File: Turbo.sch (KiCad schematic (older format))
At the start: 16 parts, among them U13 74HC74, U14 74HC86, U15 74HC74

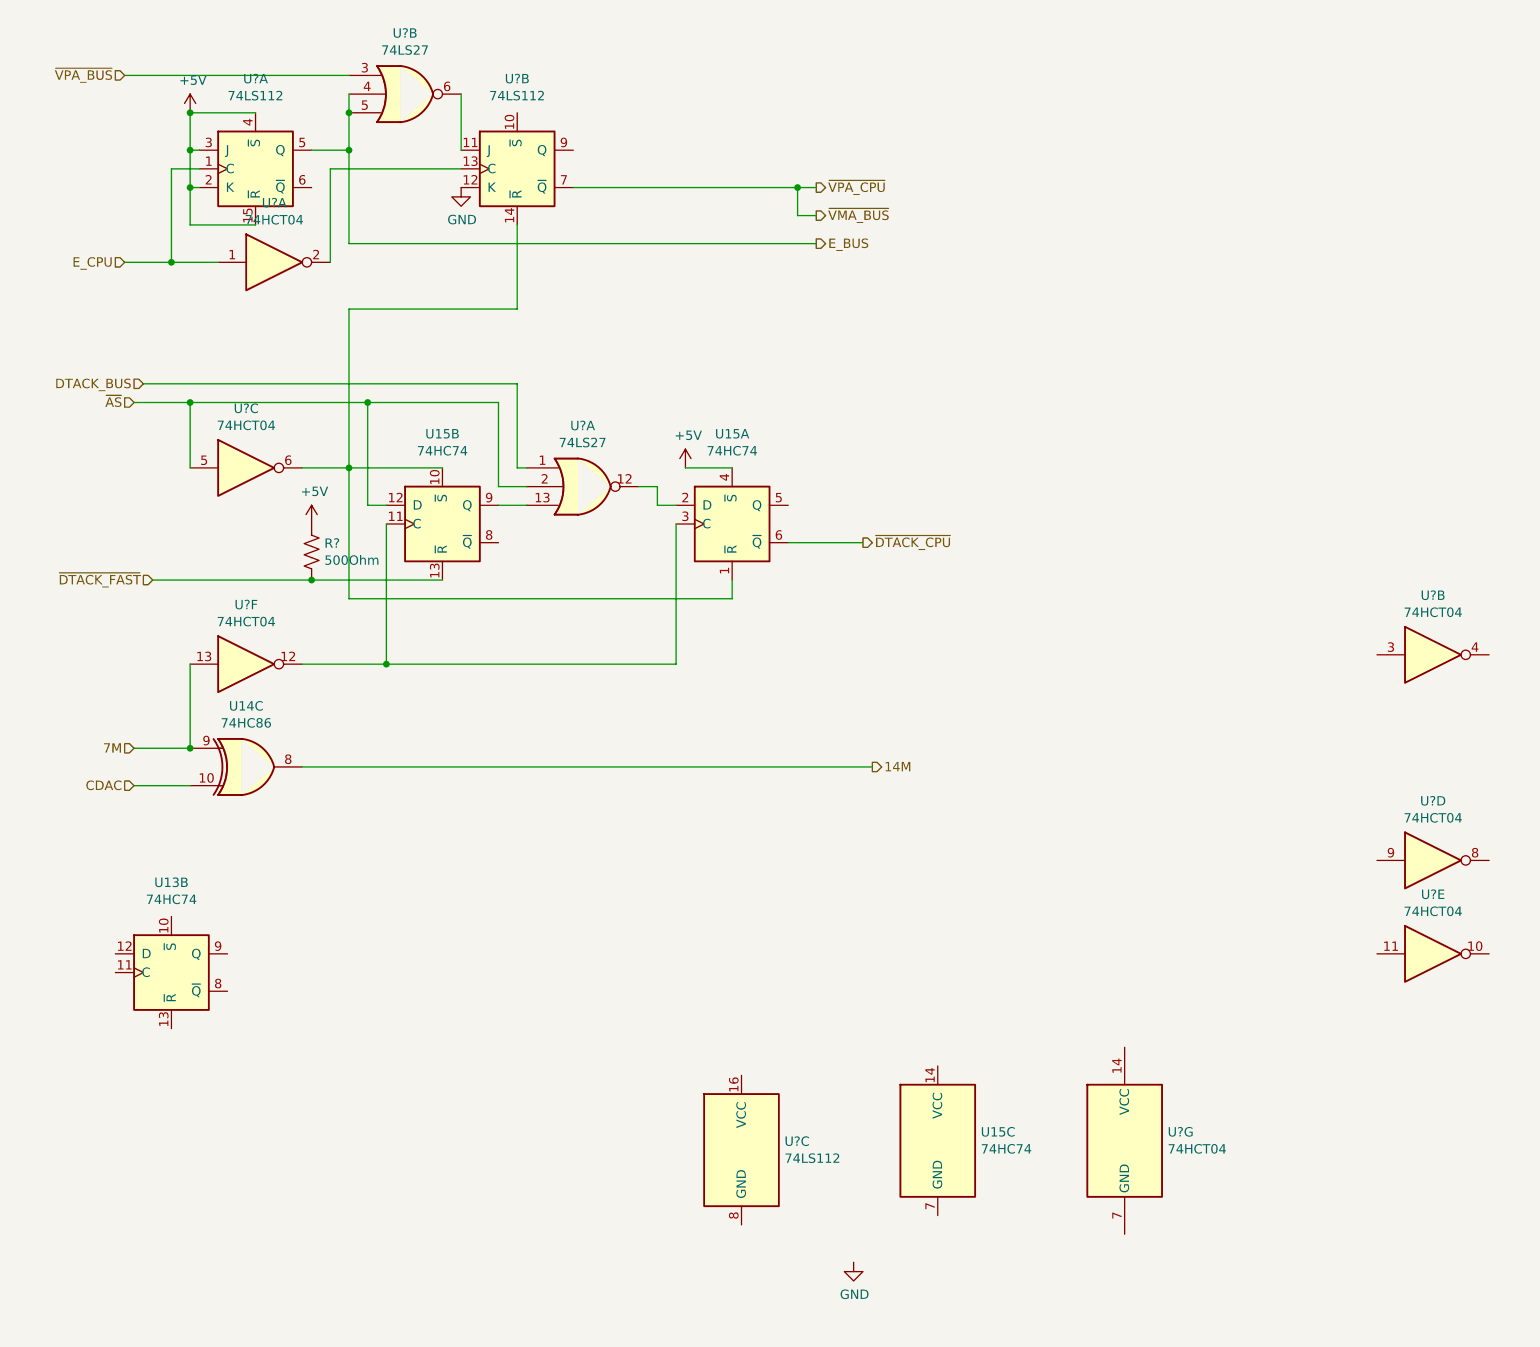
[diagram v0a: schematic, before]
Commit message: finish turbo section
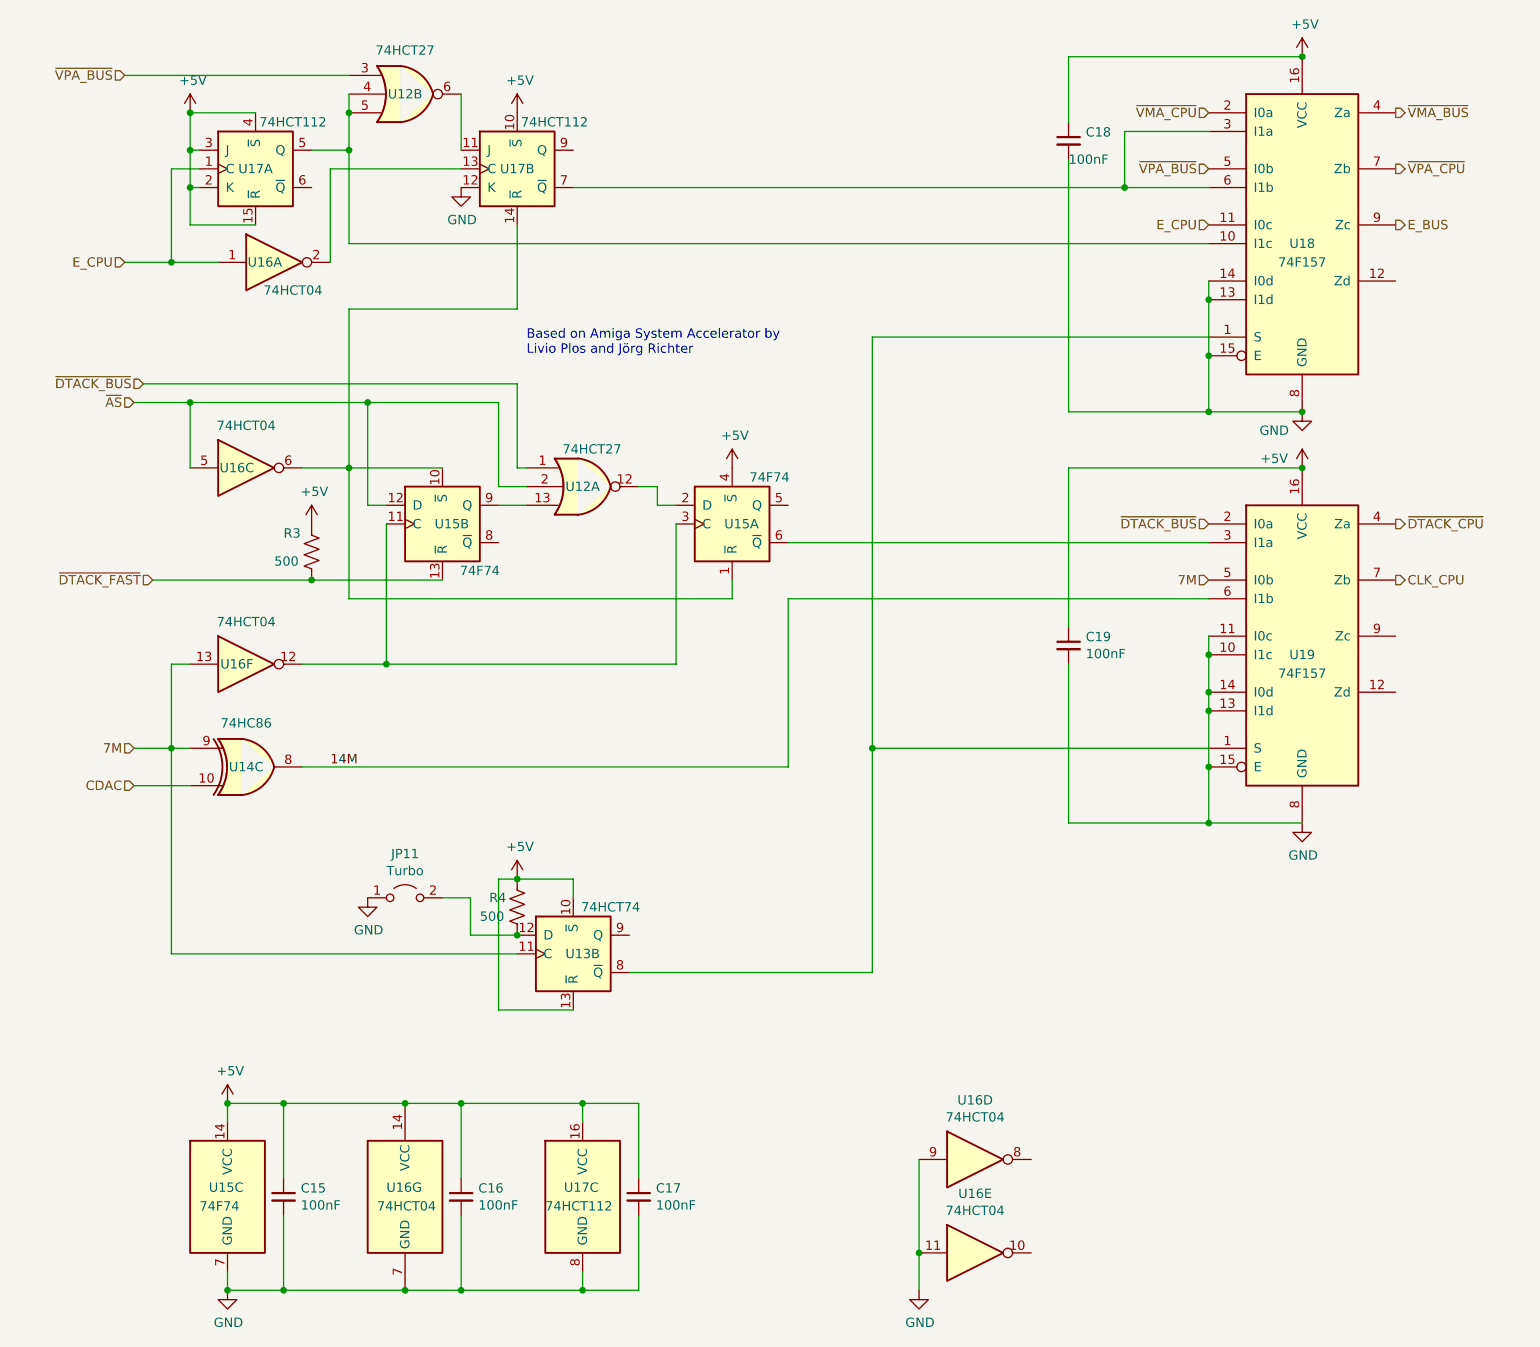
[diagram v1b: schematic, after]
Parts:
- removed U?: 74HCT04, symbol 74:74HCT04
- added C15, C16, C17, C18, C19: 100nF, symbol device:C_Small
- added JP11: Turbo, symbol jumper:Jumper_2_Open
- added R4: 500, symbol device:R_US
- added U18, U19: 74F157, symbol 74:74LS157
- R3: renamed from R?; value 500Ohm -> 500
- U12: renamed from U?; value 74LS27 -> 74HCT27
- U13: value 74HC74 -> 74HCT74
- U15: value 74HC74 -> 74F74
- U17: renamed from U?; value 74LS112 -> 74HCT112
- gave numbers to parts that had none: 1
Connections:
- net +5V: now also U13.10 (~S), U13.13 (~R), U15.14 (VCC), U16.14 (VCC), U17.10 (~S), U17.16 (VCC), C15.1, C16.1, C17.1, C18.1, C19.1, R4.1, U18.16 (VCC), U19.16 (VCC)
- net 14M: now also U19.6 (I1b)
- net 7M: now also U13.11 (C), U19.5 (I0b)
- net E_BUS: now also U18.9 (Zc); no longer U12.4, U12.5, U17.5 (Q)
- net E_CPU: now also U18.11 (I0c)
- net GND: now also U15.7 (GND), U16.11, U16.7 (GND), U16.9, U17.8 (GND), C15.2, C16.2, C17.2, C18.2, C19.2, JP11.1 (A), U18.13 (I1d), U18.14 (I0d), U18.15 (E), U18.8 (GND), U19.10 (I1c), U19.11 (I0c), U19.13 (I1d), U19.14 (I0d), U19.15 (E), U19.8 (GND)
- net ~DTACK_CPU: now also U19.4 (Za); no longer U15.6 (~Q)
- net ~VMA_BUS: now also U18.4 (Za); no longer U17.7 (~Q)
- net ~VPA_BUS: now also U18.5 (I0b)
- net at U13.12 (D): now also JP11.2 (B), R4.2
- net at U13.8 (~Q): now also U18.1 (S), U19.1 (S)
- net DTACK_BUS renamed ~DTACK_BUS
- net ~DTACK_BUS: now also U19.2 (I0a)
- new net: U15.6 (~Q), U19.3 (I1a)
- new net: U12.4, U12.5, U17.5 (Q), U18.10 (I1c)
- new net: U17.7 (~Q), U18.3 (I1a), U18.6 (I1b)
- new net CLK_CPU: U19.7 (Zb)
- new net ~VMA_CPU: U18.2 (I0a)
- new net ~VPA_CPU: U18.7 (Zb)
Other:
- note added: "Based on Amiga System Accelerator by\nLivio Plos and Jörg Richter"
- moved on the sheet: U13B, U15C, U16D, U16E, U16G, U17C

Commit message: component names
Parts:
- U14: value 74HC86 -> 74F86
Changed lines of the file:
@@
 P 1650 4700
 F 0 "U14" H 1650 4700 50  0000 C CNN
-F 1 "74HC86" H 1650 4934 50  0000 C CNN
+F 1 "74F86" H 1650 4934 50  0000 C CNN
 F 2 "" H 1650 4700 50  0001 C CNN
 F 3 "http://www.ti.com/lit/gpn/sn74HC86" H 1650 4700 50  0001 C CNN

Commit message: assign footprints
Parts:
- C15, C16, C17, C18, C19: footprint (none) -> Capacitor_THT:C_Disc_D7.0mm_W2.5mm_P5.00mm
- JP11: footprint (none) -> Connector_PinHeader_2.54mm:PinHeader_1x02_P2.54mm_Vertical
- R3, R4: footprint (none) -> Resistor_THT:R_Axial_DIN0411_L9.9mm_D3.6mm_P12.70mm_Horizontal
- U12, U13, U15, U16: footprint (none) -> Package_DIP:DIP-14_W7.62mm
- U14: footprint (none) -> Package_DIP:DIP-14_W7.62mm_Socket
- U17, U18, U19: footprint (none) -> Package_DIP:DIP-16_W7.62mm
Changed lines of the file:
@@
 F 0 "U14" H 1650 4700 50  0000 C CNN
 F 1 "74F86" H 1650 4934 50  0000 C CNN
-F 2 "" H 1650 4700 50  0001 C CNN
+F 2 "Package_DIP:DIP-14_W7.62mm_Socket" H 1650 4700 50  0001 C CNN
 F 3 "http://www.ti.com/lit/gpn/sn74HC86" H 1650 4700 50  0001 C CNN
 	3    1650 4700
@@
 F 0 "U15" H 4300 3400 50  0000 C CNN
 F 1 "74F74" H 4450 3650 50  0000 C CNN
-F 2 "" H 4250 3400 50  0001 C CNN
+F 2 "Package_DIP:DIP-14_W7.62mm" H 4250 3400 50  0001 C CNN
 F 3 "74xx/74hc_hct74.pdf" H 4250 3400 50  0001 C CNN
 	1    4250 3400
@@
 F 0 "U15" H 2750 3400 50  0000 C CNN
 F 1 "74F74" H 2900 3150 50  0000 C CNN
-F 2 "" H 2700 3400 50  0001 C CNN
+F 2 "Package_DIP:DIP-14_W7.62mm" H 2700 3400 50  0001 C CNN
 F 3 "74xx/74hc_hct74.pdf" H 2700 3400 50  0001 C CNN
 	2    2700 3400
@@
 F 0 "U15" H 1450 7050 50  0000 L CNN
 F 1 "74F74" H 1400 6950 50  0000 L CNN
-F 2 "" H 1550 7000 50  0001 C CNN
+F 2 "Package_DIP:DIP-14_W7.62mm" H 1550 7000 50  0001 C CNN
 F 3 "74xx/74hc_hct74.pdf" H 1550 7000 50  0001 C CNN
 	3    1550 7000
@@
 F 0 "U13" H 3450 5700 50  0000 C CNN
 F 1 "74HCT74" H 3600 5950 50  0000 C CNN
-F 2 "" H 3400 5700 50  0001 C CNN
+F 2 "Package_DIP:DIP-14_W7.62mm" H 3400 5700 50  0001 C CNN
 F 3 "74xx/74hc_hct74.pdf" H 3400 5700 50  0001 C CNN
 	2    3400 5700
@@
 F 0 "U16" H 1750 2000 50  0000 C CNN
 F 1 "74HCT04" H 1900 1850 50  0000 C CNN
-F 2 "" H 1800 2000 50  0001 C CNN
+F 2 "Package_DIP:DIP-14_W7.62mm" H 1800 2000 50  0001 C CNN
 F 3 "https://assets.nexperia.com/documents/data-sheet/74HC_HCT04.pdf" H 1800 2000 50  0001 C CNN
 	1    1800 2000
@@
 F 0 "U16" H 1600 3100 50  0000 C CNN
 F 1 "74HCT04" H 1650 3326 50  0000 C CNN
-F 2 "" H 1650 3100 50  0001 C CNN
+F 2 "Package_DIP:DIP-14_W7.62mm" H 1650 3100 50  0001 C CNN
 F 3 "https://assets.nexperia.com/documents/data-sheet/74HC_HCT04.pdf" H 1650 3100 50  0001 C CNN
 	3    1650 3100
@@
 F 0 "U16" H 5550 7117 50  0000 C CNN
 F 1 "74HCT04" H 5550 7026 50  0000 C CNN
-F 2 "" H 5550 6800 50  0001 C CNN
+F 2 "Package_DIP:DIP-14_W7.62mm" H 5550 6800 50  0001 C CNN
 F 3 "https://assets.nexperia.com/documents/data-sheet/74HC_HCT04.pdf" H 5550 6800 50  0001 C CNN
 	4    5550 6800
@@
 F 0 "U16" H 5550 7617 50  0000 C CNN
 F 1 "74HCT04" H 5550 7526 50  0000 C CNN
-F 2 "" H 5550 7300 50  0001 C CNN
+F 2 "Package_DIP:DIP-14_W7.62mm" H 5550 7300 50  0001 C CNN
 F 3 "https://assets.nexperia.com/documents/data-sheet/74HC_HCT04.pdf" H 5550 7300 50  0001 C CNN
 	5    5550 7300
@@
 F 0 "U16" H 1600 4150 50  0000 C CNN
 F 1 "74HCT04" H 1650 4376 50  0000 C CNN
-F 2 "" H 1650 4150 50  0001 C CNN
+F 2 "Package_DIP:DIP-14_W7.62mm" H 1650 4150 50  0001 C CNN
 F 3 "https://assets.nexperia.com/documents/data-sheet/74HC_HCT04.pdf" H 1650 4150 50  0001 C CNN
 	6    1650 4150
@@
 F 0 "U12" H 3450 3200 50  0000 C CNN
 F 1 "74HCT27" H 3500 3400 50  0000 C CNN
-F 2 "" H 3450 3200 50  0001 C CNN
+F 2 "Package_DIP:DIP-14_W7.62mm" H 3450 3200 50  0001 C CNN
 F 3 "http://www.ti.com/lit/gpn/sn74LS27" H 3450 3200 50  0001 C CNN
 	1    3450 3200
@@
 F 0 "U12" H 2500 1100 50  0000 C CNN
 F 1 "74HCT27" H 2500 1334 50  0000 C CNN
-F 2 "" H 2500 1100 50  0001 C CNN
+F 2 "Package_DIP:DIP-14_W7.62mm" H 2500 1100 50  0001 C CNN
 F 3 "http://www.ti.com/lit/gpn/sn74LS27" H 2500 1100 50  0001 C CNN
 	2    2500 1100
@@
 F 0 "R3" H 1850 3650 50  0000 L CNN
 F 1 "500" H 1800 3500 50  0000 L CNN
-F 2 "" V 2040 3540 50  0001 C CNN
+F 2 "Resistor_THT:R_Axial_DIN0411_L9.9mm_D3.6mm_P12.70mm_Horizontal" V 2040 3540 50  0001 C CNN
 F 3 "~" H 2000 3550 50  0001 C CNN
 	1    2000 3550
@@
 F 0 "U17" H 1700 1500 50  0000 C CNN
 F 1 "74HCT112" H 1900 1750 50  0000 C CNN
-F 2 "" H 1700 1500 50  0001 C CNN
+F 2 "Package_DIP:DIP-16_W7.62mm" H 1700 1500 50  0001 C CNN
 F 3 "http://www.ti.com/lit/gpn/sn74LS112" H 1700 1500 50  0001 C CNN
 	1    1700 1500
@@
 F 0 "U17" H 3100 1500 50  0000 C CNN
 F 1 "74HCT112" H 3300 1750 50  0000 C CNN
-F 2 "" H 3100 1500 50  0001 C CNN
+F 2 "Package_DIP:DIP-16_W7.62mm" H 3100 1500 50  0001 C CNN
 F 3 "http://www.ti.com/lit/gpn/sn74LS112" H 3100 1500 50  0001 C CNN
 	2    3100 1500
@@
 F 0 "U17" H 3350 7050 50  0000 L CNN
 F 1 "74HCT112" H 3250 6950 50  0000 L CNN
-F 2 "" H 3450 7000 50  0001 C CNN
+F 2 "Package_DIP:DIP-16_W7.62mm" H 3450 7000 50  0001 C CNN
 F 3 "http://www.ti.com/lit/gpn/sn74LS112" H 3450 7000 50  0001 C CNN
 	3    3450 7000
@@
 F 0 "R4" H 2950 5500 50  0000 L CNN
 F 1 "500" H 2900 5400 50  0000 L CNN
-F 2 "" V 3140 5440 50  0001 C CNN
+F 2 "Resistor_THT:R_Axial_DIN0411_L9.9mm_D3.6mm_P12.70mm_Horizontal" V 3140 5440 50  0001 C CNN
 F 3 "~" H 3100 5450 50  0001 C CNN
 	1    3100 5450
@@
 F 0 "JP11" H 2500 5635 50  0000 C CNN
 F 1 "Turbo" H 2500 5544 50  0000 C CNN
-F 2 "" H 2500 5400 50  0001 C CNN
+F 2 "Connector_PinHeader_2.54mm:PinHeader_1x02_P2.54mm_Vertical" H 2500 5400 50  0001 C CNN
 F 3 "~" H 2500 5400 50  0001 C CNN
 	1    2500 5400
@@
 F 0 "U19" H 7300 3900 50  0000 C CNN
 F 1 "74F157" H 7300 3800 50  0000 C CNN
-F 2 "" H 7300 4000 50  0001 C CNN
+F 2 "Package_DIP:DIP-16_W7.62mm" H 7300 4000 50  0001 C CNN
 F 3 "http://www.ti.com/lit/gpn/sn74LS157" H 7300 4000 50  0001 C CNN
 	1    7300 4000
@@
 F 0 "U18" H 7300 1700 50  0000 C CNN
 F 1 "74F157" H 7300 1600 50  0000 C CNN
-F 2 "" H 7300 1800 50  0001 C CNN
+F 2 "Package_DIP:DIP-16_W7.62mm" H 7300 1800 50  0001 C CNN
 F 3 "http://www.ti.com/lit/gpn/sn74LS157" H 7300 1800 50  0001 C CNN
 	1    7300 1800
@@
 F 0 "C17" H 3842 7046 50  0000 L CNN
 F 1 "100nF" H 3842 6955 50  0000 L CNN
-F 2 "" H 3750 7000 50  0001 C CNN
+F 2 "Capacitor_THT:C_Disc_D7.0mm_W2.5mm_P5.00mm" H 3750 7000 50  0001 C CNN
 F 3 "~" H 3750 7000 50  0001 C CNN
 	1    3750 7000
@@
 F 0 "C15" H 1942 7046 50  0000 L CNN
 F 1 "100nF" H 1942 6955 50  0000 L CNN
-F 2 "" H 1850 7000 50  0001 C CNN
+F 2 "Capacitor_THT:C_Disc_D7.0mm_W2.5mm_P5.00mm" H 1850 7000 50  0001 C CNN
 F 3 "~" H 1850 7000 50  0001 C CNN
 	1    1850 7000
@@
 F 0 "C16" H 2892 7046 50  0000 L CNN
 F 1 "100nF" H 2892 6955 50  0000 L CNN
-F 2 "" H 2800 7000 50  0001 C CNN
+F 2 "Capacitor_THT:C_Disc_D7.0mm_W2.5mm_P5.00mm" H 2800 7000 50  0001 C CNN
 F 3 "~" H 2800 7000 50  0001 C CNN
 	1    2800 7000
@@
 F 0 "U16" H 2400 7050 50  0000 L CNN
 F 1 "74HCT04" H 2350 6950 50  0000 L CNN
-F 2 "" H 2500 7000 50  0001 C CNN
+F 2 "Package_DIP:DIP-14_W7.62mm" H 2500 7000 50  0001 C CNN
 F 3 "https://assets.nexperia.com/documents/data-sheet/74HC_HCT04.pdf" H 2500 7000 50  0001 C CNN
 	7    2500 7000
@@
 F 0 "C18" H 6142 1396 50  0000 L CNN
 F 1 "100nF" H 6050 1250 50  0000 L CNN
-F 2 "" H 6050 1350 50  0001 C CNN
+F 2 "Capacitor_THT:C_Disc_D7.0mm_W2.5mm_P5.00mm" H 6050 1350 50  0001 C CNN
 F 3 "~" H 6050 1350 50  0001 C CNN
 	1    6050 1350
@@
 F 0 "C19" H 6142 4096 50  0000 L CNN
 F 1 "100nF" H 6142 4005 50  0000 L CNN
-F 2 "" H 6050 4050 50  0001 C CNN
+F 2 "Capacitor_THT:C_Disc_D7.0mm_W2.5mm_P5.00mm" H 6050 4050 50  0001 C CNN
 F 3 "~" H 6050 4050 50  0001 C CNN
 	1    6050 4050

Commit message: turbo layout
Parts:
- removed U14: 74F86, Package_DIP:DIP-14_W7.62mm_Socket, symbol 74:74HC86
- added U14: 74F86, Package_DIP:DIP-14_W7.62mm_Socket, symbol 74:74HC86
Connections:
- net 14M: now also U14.6
- net 7M: now also U16.3, U14.5; no longer U16.13
- net CDAC: now also U14.4
- net GND: now also U19.2 (I0a), U19.3 (I1a); no longer U19.10 (I1c), U19.11 (I0c)
- net ~DTACK_BUS: now also U19.10 (I1c); no longer U19.2 (I0a)
- net ~DTACK_CPU: now also U19.9 (Zc); no longer U19.4 (Za)
- net at U15.11 (C), U15.3 (C): now also U16.4; no longer U16.12
- net at U15.6 (~Q): now also U19.11 (I0c); no longer U19.3 (I1a)
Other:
- moved on the sheet: C19
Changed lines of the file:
@@
 Text HLabel 7800 1500 2    50   Output ~ 0
 ~VPA_CPU
-Text HLabel 7800 3400 2    50   Output ~ 0
+Text HLabel 7800 4000 2    50   Output ~ 0
 ~DTACK_CPU
 Text HLabel 1150 3700 0    50   Input ~ 0
@@
 Text HLabel 1000 2000 0    50   Input ~ 0
 E_CPU
-$Comp
-L 74:74HC86 U14
-U 3 1 606BF6DE
-P 1650 4700
-F 0 "U14" H 1650 4700 50  0000 C CNN
-F 1 "74F86" H 1650 4934 50  0000 C CNN
-F 2 "Package_DIP:DIP-14_W7.62mm_Socket" H 1650 4700 50  0001 C CNN
-F 3 "http://www.ti.com/lit/gpn/sn74HC86" H 1650 4700 50  0001 C CNN
-	3    1650 4700
-	1    0    0    -1
-$EndComp
 Wire Wire Line
 	1050 4600 1250 4600
@@
 $Comp
 L 74:74HCT04 U16
-U 6 1 606DFD1C
+U 2 1 606DFD1C
 P 1650 4150
 F 0 "U16" H 1600 4150 50  0000 C CNN
@@
 F 2 "Package_DIP:DIP-14_W7.62mm" H 1650 4150 50  0001 C CNN
 F 3 "https://assets.nexperia.com/documents/data-sheet/74HC_HCT04.pdf" H 1650 4150 50  0001 C CNN
-	6    1650 4150
+	2    1650 4150
 	1    0    0    -1
 $EndComp
@@
 	2200 1900 6800 1900
 Wire Wire Line
-	4550 3500 6800 3500
+	4550 3500 6600 3500
 Wire Wire Line
 	4550 3800 6800 3800
 Wire Wire Line
 	4550 3800 4550 4700
-Wire Wire Line
-	6800 4000 6800 4100
 Connection ~ 6800 4700
-Connection ~ 6800 4100
-Wire Wire Line
-	6800 4100 6800 4300
-Connection ~ 6800 4300
 Wire Wire Line
 	6800 4300 6800 4400
@@
 Text HLabel 6800 3700 0    50   Input ~ 0
 7M
-Text HLabel 6800 3400 0    50   Input ~ 0
+Text HLabel 6800 4100 0    50   Input ~ 0
 ~DTACK_BUS
 Text HLabel 6800 1500 0    50   Input ~ 0
@@
 L device:C_Small C19
 U 1 1 5FFA80E0
-P 6050 4050
-F 0 "C19" H 6142 4096 50  0000 L CNN
-F 1 "100nF" H 6142 4005 50  0000 L CNN
-F 2 "Capacitor_THT:C_Disc_D7.0mm_W2.5mm_P5.00mm" H 6050 4050 50  0001 C CNN
-F 3 "~" H 6050 4050 50  0001 C CNN
-	1    6050 4050
+P 6050 3200
+F 0 "C19" H 6142 3246 50  0000 L CNN
+F 1 "100nF" H 6142 3155 50  0000 L CNN
+F 2 "Capacitor_THT:C_Disc_D7.0mm_W2.5mm_P5.00mm" H 6050 3200 50  0001 C CNN
+F 3 "~" H 6050 3200 50  0001 C CNN
+	1    6050 3200
 	1    0    0    -1
 $EndComp
@@
 	5000 2400 6800 2400
 Wire Wire Line
-	6050 4150 6050 5000
-Wire Wire Line
 	6050 5000 6800 5000
 Connection ~ 6800 5000
@@
 Connection ~ 7300 3100
 Wire Wire Line
-	6050 3100 6050 3950
-Wire Wire Line
 	6350 1600 6350 1300
 Connection ~ 6350 1600
@@
 	6050 2800 6800 2800
 Connection ~ 6800 2800
+$Comp
+L 74:74HC86 U?
+U 2 1 6045D239
+P 1650 4700
+AR Path="/6068F728/6045D239" Ref="U?"  Part="2"
+AR Path="/606B7AE6/6045D239" Ref="U14"  Part="2"
+F 0 "U14" H 1650 4700 50  0000 C CNN
+F 1 "74F86" H 1650 4934 50  0000 C CNN
+F 2 "Package_DIP:DIP-14_W7.62mm_Socket" H 1650 4700 50  0001 C CNN
+F 3 "http://www.ti.com/lit/gpn/sn74HC86" H 1650 4700 50  0001 C CNN
+	2    1650 4700
+	1    0    0    1
+$EndComp
+Wire Wire Line
+	6800 4000 6600 4000
+Wire Wire Line
+	6600 4000 6600 3500
+Wire Wire Line
+	6050 3300 6050 3400
+Wire Wire Line
+	6050 3400 6800 3400
+Connection ~ 6050 3400
+Wire Wire Line
+	6050 3400 6050 5000
+Wire Wire Line
+	6800 3500 6800 3400
+Connection ~ 6800 3400
 $EndSCHEMATC
